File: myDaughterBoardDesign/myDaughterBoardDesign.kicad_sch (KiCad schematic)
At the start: 2 parts, among them J1 DaughterBoard, U1 PCA9685PW

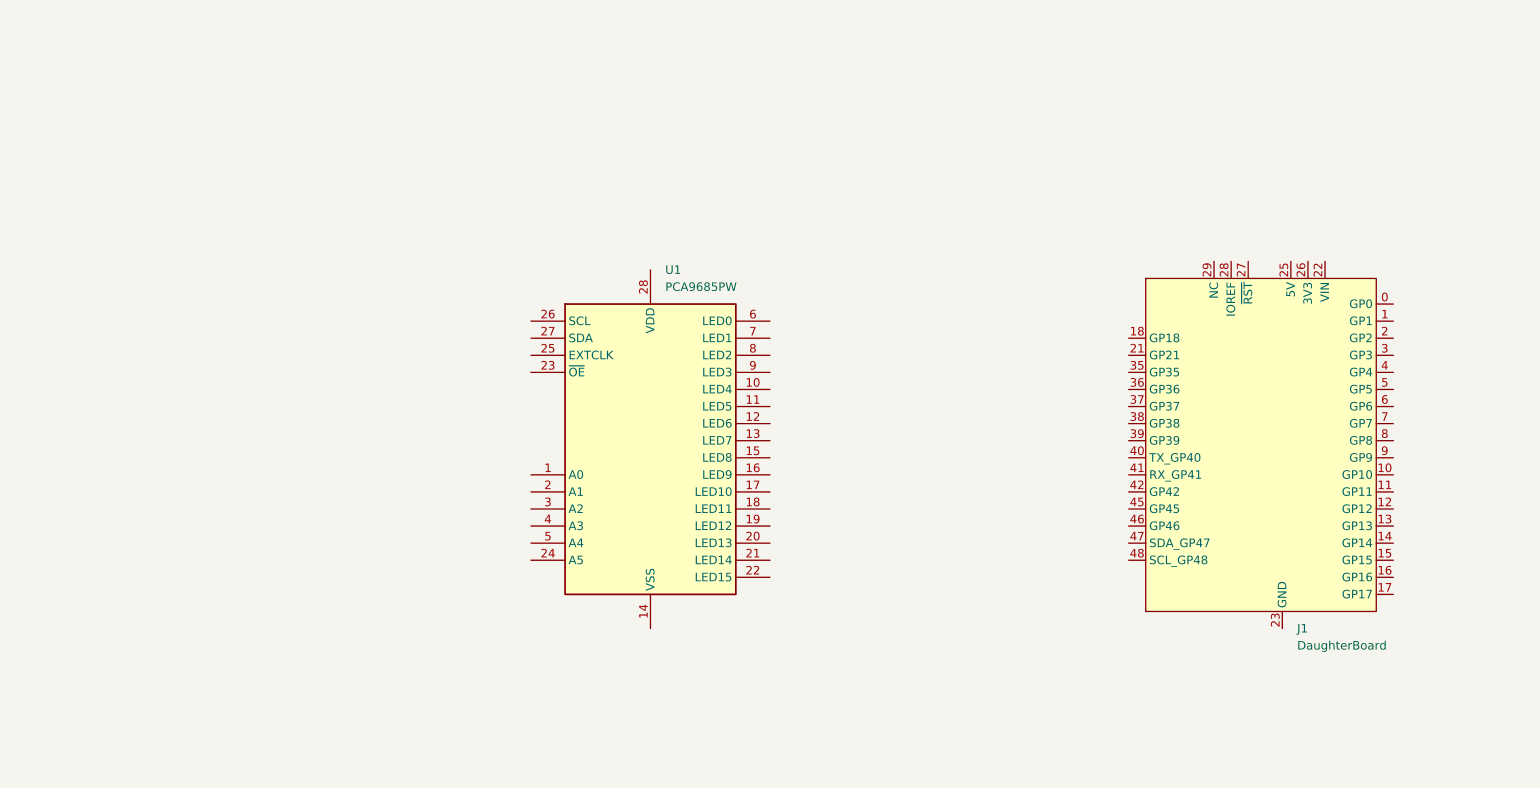
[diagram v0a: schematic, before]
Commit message: Sat: Apr 27 Added Dual H-Bridge Daughterboard and fixed railsplitter
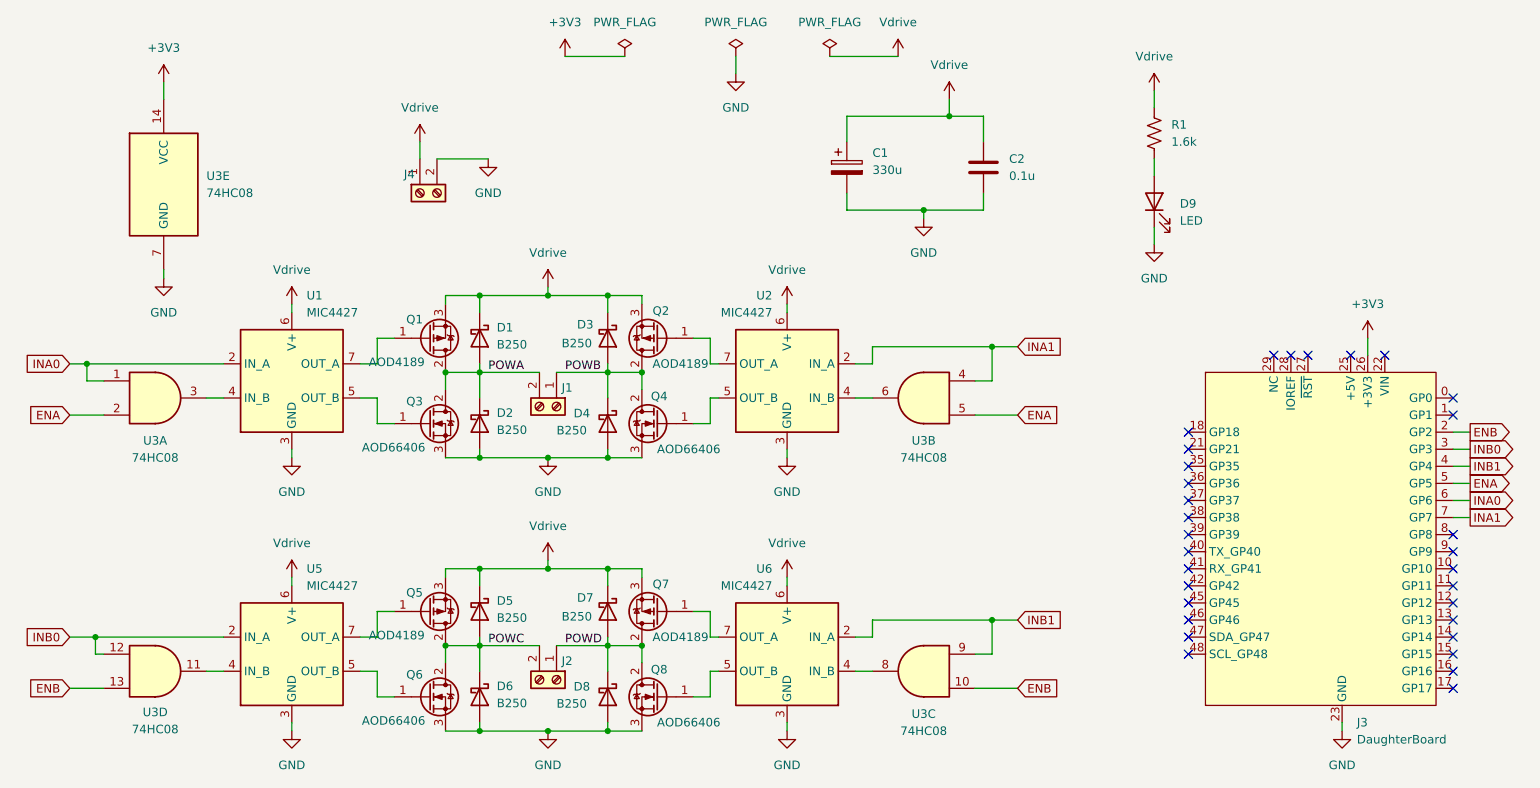
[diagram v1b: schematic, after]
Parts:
- removed J1: DaughterBoard, myparts:DaughterBoardTemplate, symbol myparts:DaughterBoard
- removed U1: PCA9685PW, Package_SO:TSSOP-28_4.4x9.7mm_P0.65mm, symbol Driver_LED:PCA9685PW
- added C1: 330u, Capacitor_SMD:CP_Elec_8x10, symbol Device:C_Polarized
- added C2: 0.1u, Capacitor_SMD:C_1206_3216Metric_Pad1.33x1.80mm_HandSolder, symbol Device:C
- added D1, D2, D3, D4, D5, D6, D7, D8: B250, Diode_SMD:D_SMB, symbol Diode:B250
- added D9: LED, LED_SMD:LED_1206_3216Metric_Pad1.42x1.75mm_HandSolder, symbol Device:LED
- added J1, J2, J4: Screw_Terminal_01x02, TerminalBlock:TerminalBlock_Altech_AK300-2_P5.00mm, symbol Connector:Screw_Terminal_01x02
- added J3: DaughterBoard, myparts:DaughterBoardTemplate, symbol myparts:DaughterBoard
- added Q1, Q2, Q5, Q7: AOD4189, Package_TO_SOT_SMD:TO-252-2, symbol myparts:AOD4189
- added Q3, Q4, Q6, Q8: AOD66406, Package_TO_SOT_SMD:TO-252-2, symbol myparts:AOD66406
- added R1: 1.6k, Resistor_SMD:R_1206_3216Metric_Pad1.30x1.75mm_HandSolder, symbol Device:R_US
- added U1, U2, U5, U6: MIC4427, Package_SO:SO-8_3.9x4.9mm_P1.27mm, symbol Driver_FET:MIC4427
- added U3: 74HC08, Package_SO:SO-14_3.9x8.65mm_P1.27mm, symbol myparts:74HC08
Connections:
- net GND: now also C1.2, C2.2, D2.2 (A), D4.2 (A), D6.2 (A), D8.2 (A), D9.1 (K), J3.23 (GND), J3.24 (GND), J3.30 (GND), J4.2 (Pin_2), Q3.3 (S), Q4.3 (S), Q6.3 (S), Q8.3 (S), U1.3 (GND), U2.3 (GND), U3.7 (GND), U5.3 (GND), U6.3 (GND)
- new net: U1.4 (IN_B), U3.3
- new net: Q3.1 (G), U1.5 (OUT_B)
- new net: Q1.1 (G), U1.7 (OUT_A)
- new net: D9.2 (A), R1.2
- new net: U3.8, U6.4 (IN_B)
- new net: Q8.1 (G), U6.5 (OUT_B)
- new net: Q7.1 (G), U6.7 (OUT_A)
- new net: U2.4 (IN_B), U3.6
- new net: Q4.1 (G), U2.5 (OUT_B)
- new net: Q2.1 (G), U2.7 (OUT_A)
- new net: Q5.1 (G), U5.7 (OUT_A)
- new net: Q6.1 (G), U5.5 (OUT_B)
- new net: U3.11, U5.4 (IN_B)
- new net +3V3: J3.26 (+3V3), J3.32 (+3V3), U3.14 (VCC)
- new net ENA: J3.5 (GP5), U3.2, U3.5
- new net ENB: J3.2 (GP2), U3.10, U3.13
- new net INA0: J3.6 (GP6), U1.2 (IN_A), U3.1
- new net INA1: J3.7 (GP7), U2.2 (IN_A), U3.4
- new net INB0: J3.3 (GP3), U3.12, U5.2 (IN_A)
- new net INB1: J3.4 (GP4), U3.9, U6.2 (IN_A)
- new net POWA: D1.2 (A), D2.1 (K), J1.2 (Pin_2), Q1.2 (D), Q3.2 (D)
- new net POWB: D3.2 (A), D4.1 (K), J1.1 (Pin_1), Q2.2 (D), Q4.2 (D)
- new net POWC: D5.2 (A), D6.1 (K), J2.2 (Pin_2), Q5.2 (D), Q6.2 (D)
- new net POWD: D7.2 (A), D8.1 (K), J2.1 (Pin_1), Q7.2 (D), Q8.2 (D)
- new net Vdrive: C1.1, C2.1, D1.1 (K), D3.1 (K), D5.1 (K), D7.1 (K), J4.1 (Pin_1), Q1.3 (S), Q2.3 (S), Q5.3 (S), Q7.3 (S), R1.1, U1.6 (V+), U2.6 (V+), U5.6 (V+), U6.6 (V+)
- no-connect marks 0 -> 31
